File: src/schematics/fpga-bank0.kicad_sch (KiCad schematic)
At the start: 5 parts, among them U6 LFE5U-85F-*BG756*

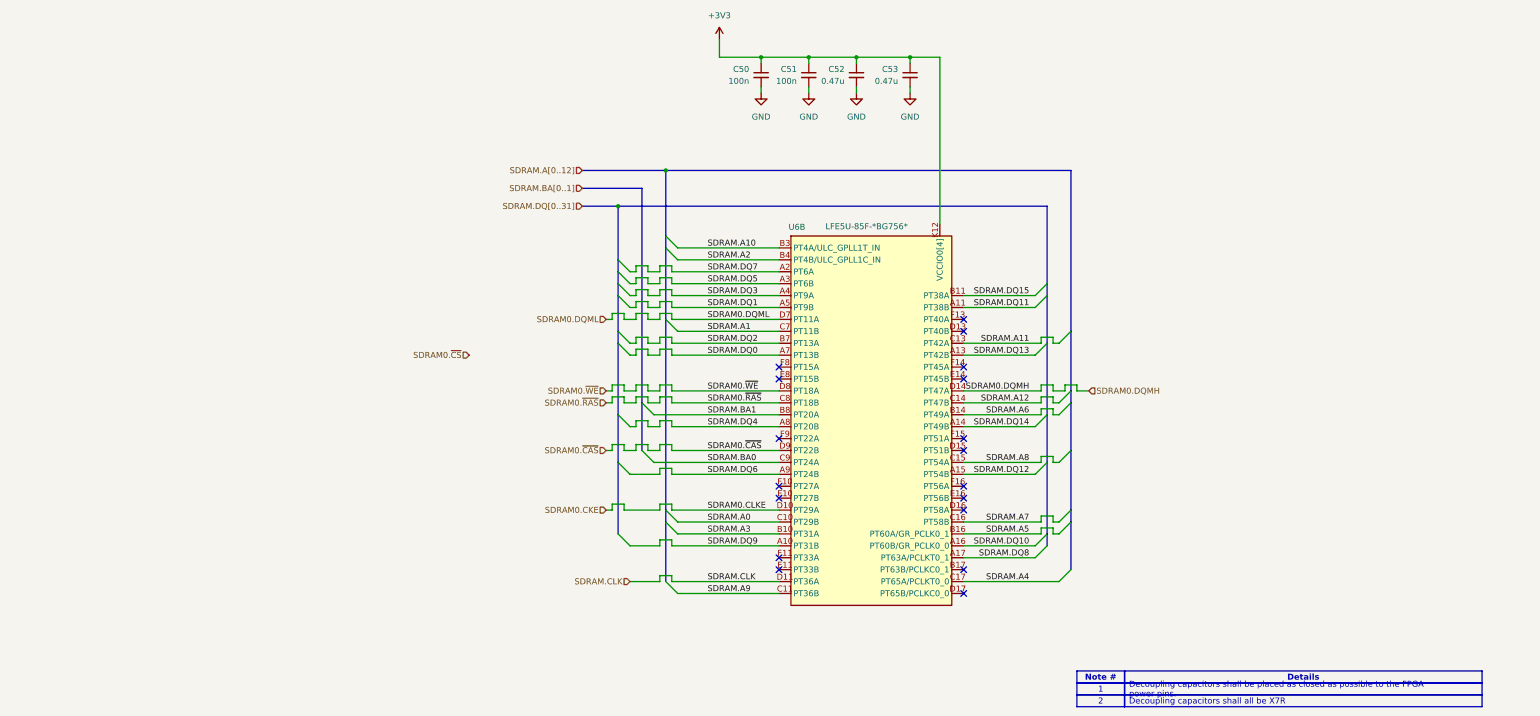
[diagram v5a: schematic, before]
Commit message: Add length matching for the emmc
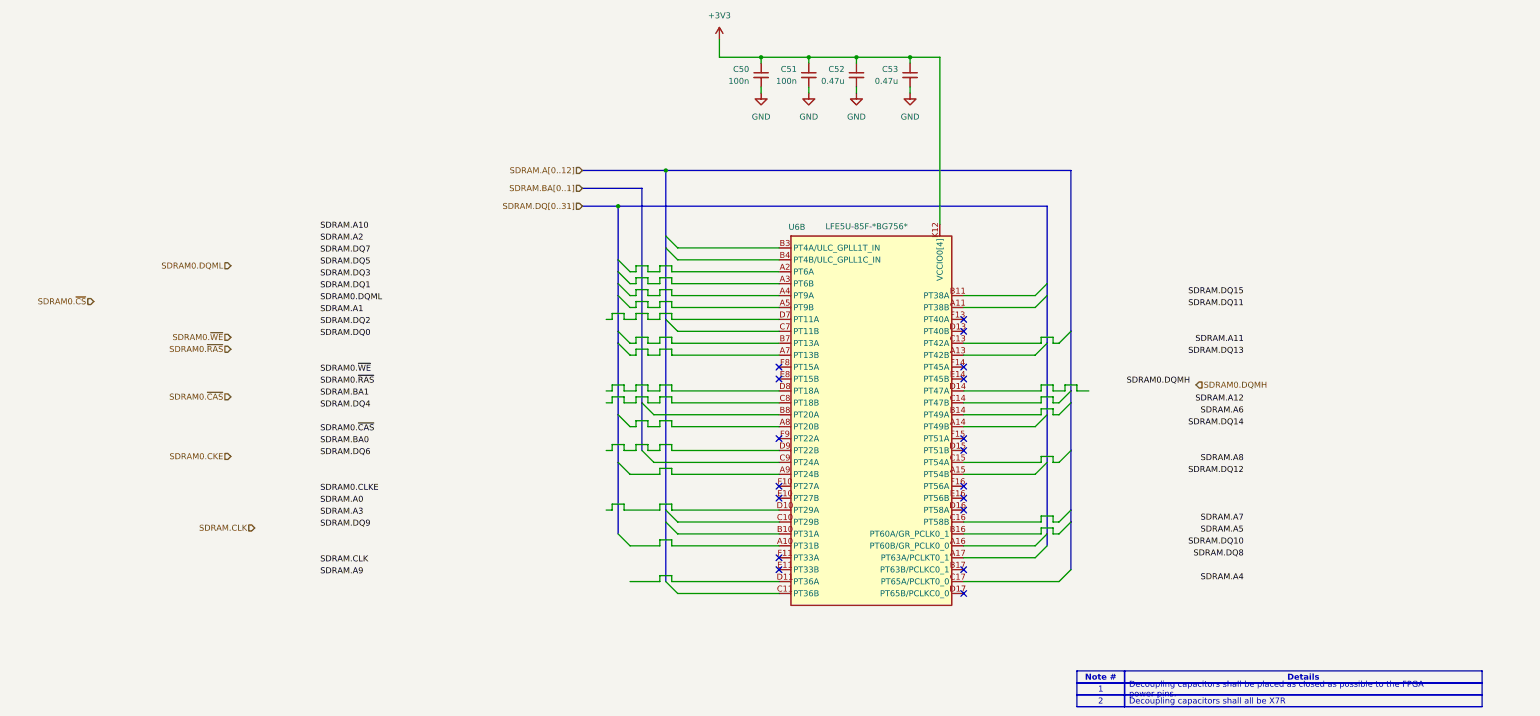
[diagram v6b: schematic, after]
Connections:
- net SDRAM.A0: no longer U6.C10 (PT29B)
- net SDRAM.A1: no longer U6.C7 (PT11B)
- net SDRAM.A10: no longer U6.B3 (PT4A/ULC_GPLL1T_IN)
- net SDRAM.A11: no longer U6.C13 (PT42A)
- net SDRAM.A12: no longer U6.C14 (PT47B)
- net SDRAM.A2: no longer U6.B4 (PT4B/ULC_GPLL1C_IN)
- net SDRAM.A3: no longer U6.B10 (PT31A)
- net SDRAM.A4: no longer U6.C17 (PT65A/PCLKT0_0)
- net SDRAM.A5: no longer U6.B16 (PT60A/GR_PCLK0_1)
- net SDRAM.A6: no longer U6.B14 (PT49A)
- net SDRAM.A7: no longer U6.C16 (PT58B)
- net SDRAM.A8: no longer U6.C15 (PT54A)
- net SDRAM.A9: no longer U6.C11 (PT36B)
- net SDRAM.BA0: no longer U6.C9 (PT24A)
- net SDRAM.BA1: no longer U6.B8 (PT20A)
- net SDRAM.CLK: no longer U6.D11 (PT36A)
- net SDRAM.DQ0: no longer U6.A7 (PT13B)
- net SDRAM.DQ1: no longer U6.A5 (PT9B)
- net SDRAM.DQ10: no longer U6.A16 (PT60B/GR_PCLK0_0)
- net SDRAM.DQ11: no longer U6.A11 (PT38B)
- net SDRAM.DQ12: no longer U6.A15 (PT54B)
- net SDRAM.DQ13: no longer U6.A13 (PT42B)
- net SDRAM.DQ14: no longer U6.A14 (PT49B)
- net SDRAM.DQ15: no longer U6.B11 (PT38A)
- net SDRAM.DQ2: no longer U6.B7 (PT13A)
- net SDRAM.DQ3: no longer U6.A4 (PT9A)
- net SDRAM.DQ4: no longer U6.A8 (PT20B)
- net SDRAM.DQ5: no longer U6.A3 (PT6B)
- net SDRAM.DQ6: no longer U6.A9 (PT24B)
- net SDRAM.DQ7: no longer U6.A2 (PT6A)
- net SDRAM.DQ8: no longer U6.A17 (PT63A/PCLKT0_1)
- net SDRAM.DQ9: no longer U6.A10 (PT31B)
- net SDRAM0.CKE: no longer U6.D10 (PT29A)
- net SDRAM0.DQMH: no longer U6.D14 (PT47A)
- net SDRAM0.DQML: no longer U6.D7 (PT11A)
- net SDRAM0.~{CAS}: no longer U6.D9 (PT22B)
- net SDRAM0.~{RAS}: no longer U6.C8 (PT18B)
- net SDRAM0.~{WE}: no longer U6.D8 (PT18A)
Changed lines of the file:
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@@
 	)
 	(label "SDRAM.A11"
-		(at 182.88 92.71 180)
+		(at 228.6 92.71 180)
 		(effects
 			(font
@@
 	)
 	(label "SDRAM.A8"
-		(at 182.88 118.11 180)
+		(at 228.6 118.11 180)
 		(effects
 			(font
@@
 	)
 	(label "SDRAM.A5"
-		(at 182.88 133.35 180)
+		(at 228.6 133.35 180)
 		(effects
 			(font
@@
 	)
 	(label "SDRAM0.DQMH"
-		(at 182.88 102.87 180)
+		(at 217.17 101.6 180)
 		(effects
 			(font
@@
 	)
 	(label "SDRAM.DQ5"
-		(at 114.3 80.01 0)
+		(at 31.75 76.2 0)
 		(effects
 			(font
@@
 	)
 	(label "SDRAM0.~{RAS}"
-		(at 114.3 105.41 0)
+		(at 31.75 101.6 0)
 		(effects
 			(font
@@
 	)
 	(label "SDRAM.A9"
-		(at 114.3 146.05 0)
+		(at 31.75 142.24 0)
 		(effects
 			(font
@@
 	)
 	(label "SDRAM.CLK"
-		(at 114.3 143.51 0)
+		(at 31.75 139.7 0)
 		(effects
 			(font
@@
 	)
 	(label "SDRAM.DQ14"
-		(at 182.88 110.49 180)
+		(at 228.6 110.49 180)
 		(effects
 			(font
@@
 	)
 	(label "SDRAM.DQ1"
-		(at 114.3 85.09 0)
+		(at 31.75 81.28 0)
 		(effects
 			(font
@@
 	)
 	(label "SDRAM0.~{CAS}"
-		(at 114.3 115.57 0)
+		(at 31.75 111.76 0)
 		(effects
 			(font
@@
 	)
 	(label "SDRAM.DQ11"
-		(at 182.88 85.09 180)
+		(at 228.6 85.09 180)
 		(effects
 			(font
@@
 	)
 	(label "SDRAM.A12"
-		(at 182.88 105.41 180)
+		(at 228.6 105.41 180)
 		(effects
 			(font
@@
 	)
 	(label "SDRAM.DQ10"
-		(at 182.88 135.89 180)
+		(at 228.6 135.89 180)
 		(effects
 			(font
@@
 	)
 	(label "SDRAM.DQ8"
-		(at 182.88 138.43 180)
+		(at 228.6 138.43 180)
 		(effects
 			(font
@@
 	)
 	(label "SDRAM0.CLKE"
-		(at 114.3 128.27 0)
+		(at 31.75 124.46 0)
 		(effects
 			(font
@@
 	)
 	(label "SDRAM.A6"
-		(at 182.88 107.95 180)
+		(at 228.6 107.95 180)
 		(effects
 			(font
@@
 	)
 	(label "SDRAM.DQ13"
-		(at 182.88 95.25 180)
+		(at 228.6 95.25 180)
 		(effects
 			(font
@@
 	)
 	(label "SDRAM.A10"
-		(at 114.3 72.39 0)
+		(at 31.75 68.58 0)
 		(effects
 			(font
@@
 	)
 	(label "SDRAM.DQ0"
-		(at 114.3 95.25 0)
+		(at 31.75 91.44 0)
 		(effects
 			(font
@@
 	)
 	(label "SDRAM.DQ12"
-		(at 182.88 120.65 180)
+		(at 228.6 120.65 180)
 		(effects
 			(font
@@
 	)
 	(label "SDRAM0.~{WE}"
-		(at 114.3 102.87 0)
+		(at 31.75 99.06 0)
 		(effects
 			(font
@@
 	)
 	(label "SDRAM.BA1"
-		(at 114.3 107.95 0)
+		(at 31.75 104.14 0)
 		(effects
 			(font
@@
 	)
 	(label "SDRAM.DQ3"
-		(at 114.3 82.55 0)
+		(at 31.75 78.74 0)
 		(effects
 			(font
@@
 	)
 	(label "SDRAM.A2"
-		(at 114.3 74.93 0)
+		(at 31.75 71.12 0)
 		(effects
 			(font
@@
 	)
 	(label "SDRAM.DQ9"
-		(at 114.3 135.89 0)
+		(at 31.75 132.08 0)
 		(effects
 			(font
@@
 	)
 	(label "SDRAM.A7"
-		(at 182.88 130.81 180)
+		(at 228.6 130.81 180)
 		(effects
 			(font
@@
 	)
 	(label "SDRAM0.DQML"
-		(at 114.3 87.63 0)
+		(at 31.75 83.82 0)
 		(effects
 			(font
@@
 	)
 	(label "SDRAM.BA0"
-		(at 114.3 118.11 0)
+		(at 31.75 114.3 0)
 		(effects
 			(font
@@
 	)
 	(label "SDRAM.A4"
-		(at 182.88 143.51 180)
+		(at 228.6 143.51 180)
 		(effects
 			(font
@@
 	)
 	(label "SDRAM.A1"
-		(at 114.3 90.17 0)
+		(at 31.75 86.36 0)
 		(effects
 			(font
@@
 	)
 	(label "SDRAM.DQ7"
-		(at 114.3 77.47 0)
+		(at 31.75 73.66 0)
 		(effects
 			(font
@@
 	)
 	(label "SDRAM.DQ6"
-		(at 114.3 120.65 0)
+		(at 31.75 116.84 0)
 		(effects
 			(font
@@
 	)
 	(label "SDRAM.DQ2"
-		(at 114.3 92.71 0)
+		(at 31.75 88.9 0)
 		(effects
 			(font
@@
 	)
 	(label "SDRAM.DQ4"
-		(at 114.3 110.49 0)
+		(at 31.75 106.68 0)
 		(effects
 			(font
@@
 	)
 	(label "SDRAM.DQ15"
-		(at 182.88 82.55 180)
+		(at 228.6 82.55 180)
 		(effects
 			(font
@@
 	)
 	(label "SDRAM.A3"
-		(at 114.3 133.35 0)
+		(at 31.75 129.54 0)
 		(effects
 			(font
@@
 	)
 	(label "SDRAM.A0"
-		(at 114.3 130.81 0)
+		(at 31.75 127 0)
 		(effects
 			(font
@@
 	(hierarchical_label "SDRAM0.~{CS}"
 		(shape input)
-		(at 63.5 95.25 180)
+		(at -16.51 83.82 180)
 		(effects
 			(font
@@
 	(hierarchical_label "SDRAM0.~{WE}"
 		(shape input)
-		(at 92.71 102.87 180)
+		(at 12.7 91.44 180)
 		(effects
 			(font
@@
 	(hierarchical_label "SDRAM.CLK"
 		(shape input)
-		(at 97.79 143.51 180)
+		(at 17.78 132.08 180)
 		(effects
 			(font
@@
 	(hierarchical_label "SDRAM0.~{RAS}"
 		(shape input)
-		(at 92.71 105.41 180)
+		(at 12.7 93.98 180)
 		(effects
 			(font
@@
 	(hierarchical_label "SDRAM0.~{CAS}"
 		(shape input)
-		(at 92.71 115.57 180)
+		(at 12.7 104.14 180)
 		(effects
 			(font
@@
 	(hierarchical_label "SDRAM0.DQML"
 		(shape input)
-		(at 92.71 87.63 180)
+		(at 12.7 76.2 180)
 		(effects
 			(font
@@
 	(hierarchical_label "SDRAM0.CKE"
 		(shape input)
-		(at 92.71 128.27 180)
+		(at 12.7 116.84 180)
 		(effects
 			(font
@@
 	(hierarchical_label "SDRAM0.DQMH"
 		(shape input)
-		(at 195.58 102.87 0)
-		(effects
-			(font
+		(at 218.44 101.6 0)
+		(effects
+			(font

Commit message: Start routing the sdrams
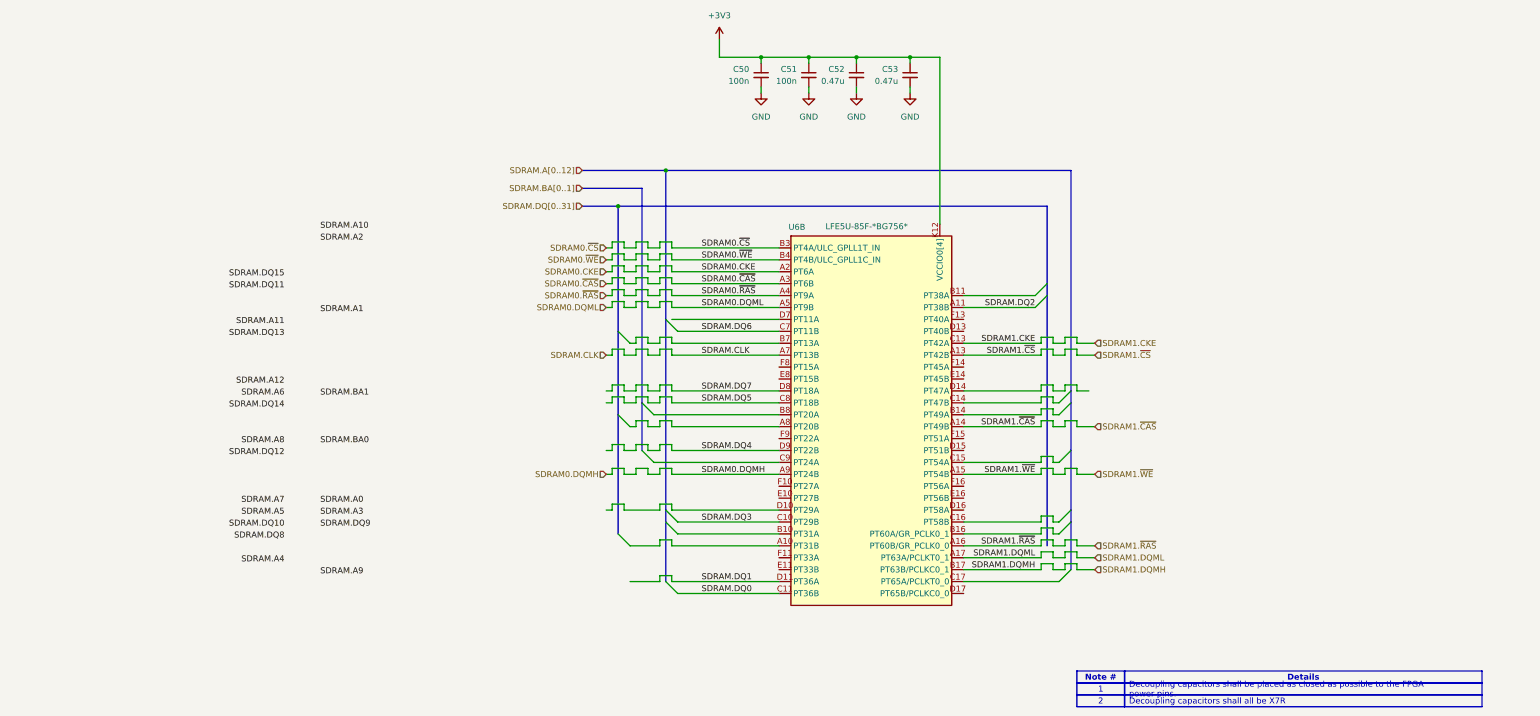
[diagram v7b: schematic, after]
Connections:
- net SDRAM.CLK: now also U6.A7 (PT13B)
- net SDRAM.DQ0: now also U6.C11 (PT36B)
- net SDRAM.DQ1: now also U6.D11 (PT36A)
- net SDRAM.DQ2: now also U6.A11 (PT38B)
- net SDRAM.DQ3: now also U6.C10 (PT29B)
- net SDRAM.DQ4: now also U6.D9 (PT22B)
- net SDRAM.DQ5: now also U6.C8 (PT18B)
- net SDRAM.DQ6: now also U6.C7 (PT11B)
- net SDRAM.DQ7: now also U6.D8 (PT18A)
- net SDRAM0.CKE: now also U6.A2 (PT6A)
- net SDRAM0.DQMH: now also U6.A9 (PT24B)
- net SDRAM0.DQML: now also U6.A5 (PT9B)
- net SDRAM0.~{CAS}: now also U6.A3 (PT6B)
- net SDRAM0.~{CS}: now also U6.B3 (PT4A/ULC_GPLL1T_IN)
- net SDRAM0.~{RAS}: now also U6.A4 (PT9A)
- net SDRAM0.~{WE}: now also U6.B4 (PT4B/ULC_GPLL1C_IN)
- net SDRAM1.~{CS}: now reaches U6.A13 (PT42B)
- net SDRAM1.~{CAS}: now reaches U6.A14 (PT49B)
- net SDRAM1.~{WE}: now reaches U6.A15 (PT54B)
- net SDRAM1.~{RAS}: now reaches U6.A16 (PT60B/GR_PCLK0_0)
- net SDRAM1.DQML: now reaches U6.A17 (PT63A/PCLKT0_1)
- net SDRAM1.DQMH: now reaches U6.B17 (PT63B/PCLKC0_1)
- net SDRAM1.CKE: now reaches U6.C13 (PT42A)
- no-connect marks 18 -> 0

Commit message: Finish routing the traces for the sdram
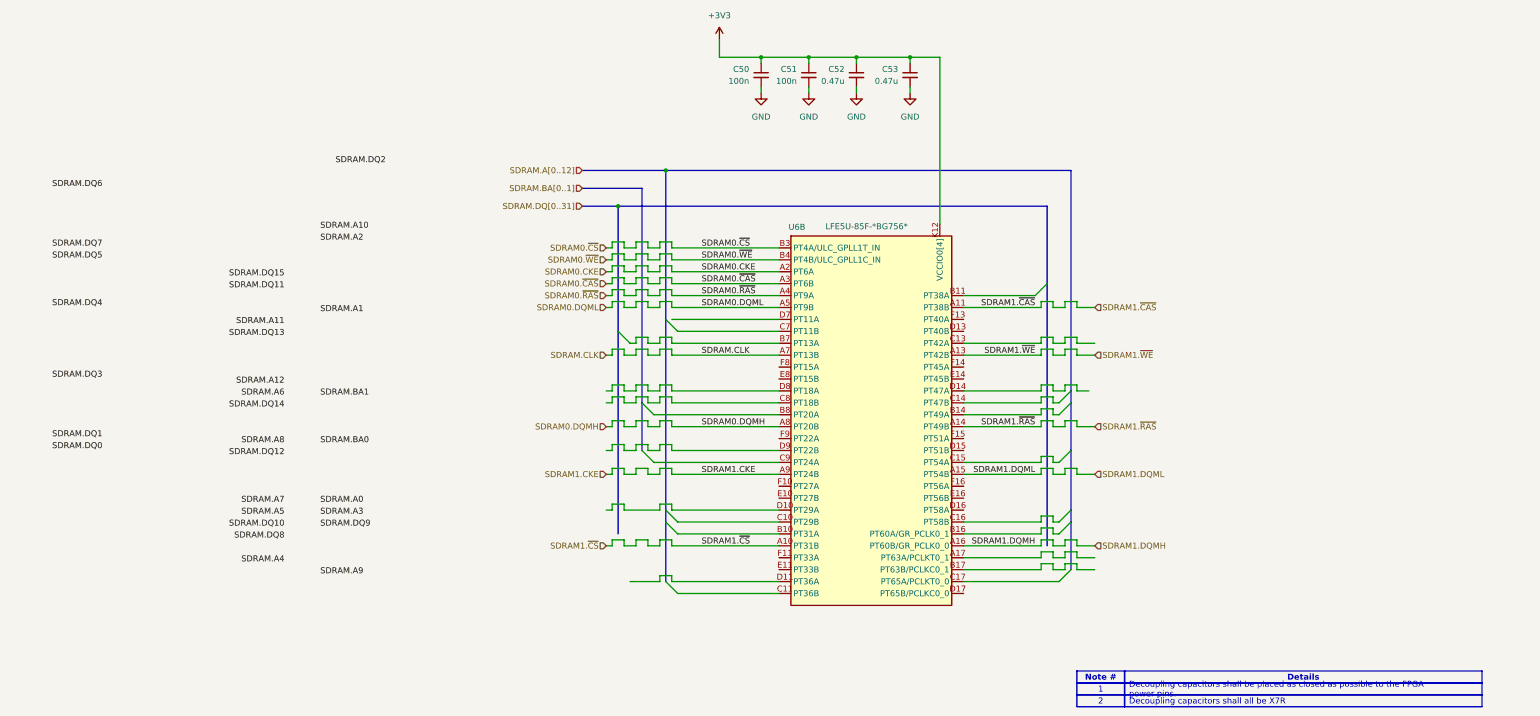
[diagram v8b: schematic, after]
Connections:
- net SDRAM.DQ0: no longer U6.C11 (PT36B)
- net SDRAM.DQ1: no longer U6.D11 (PT36A)
- net SDRAM.DQ2: no longer U6.A11 (PT38B)
- net SDRAM.DQ3: no longer U6.C10 (PT29B)
- net SDRAM.DQ4: no longer U6.D9 (PT22B)
- net SDRAM.DQ5: no longer U6.C8 (PT18B)
- net SDRAM.DQ6: no longer U6.C7 (PT11B)
- net SDRAM.DQ7: no longer U6.D8 (PT18A)
- net SDRAM0.DQMH: now also U6.A8 (PT20B); no longer U6.A9 (PT24B)
- net SDRAM1.CKE: now also U6.A9 (PT24B); no longer U6.C13 (PT42A)
- net SDRAM1.DQMH: now also U6.A16 (PT60B/GR_PCLK0_0); no longer U6.B17 (PT63B/PCLKC0_1)
- net SDRAM1.DQML: now also U6.A15 (PT54B); no longer U6.A17 (PT63A/PCLKT0_1)
- net SDRAM1.~{CAS}: now also U6.A11 (PT38B); no longer U6.A14 (PT49B)
- net SDRAM1.~{CS}: now also U6.A10 (PT31B); no longer U6.A13 (PT42B)
- net SDRAM1.~{RAS}: now also U6.A14 (PT49B); no longer U6.A16 (PT60B/GR_PCLK0_0)
- net SDRAM1.~{WE}: now also U6.A13 (PT42B); no longer U6.A15 (PT54B)
